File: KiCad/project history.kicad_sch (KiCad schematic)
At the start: 0 parts

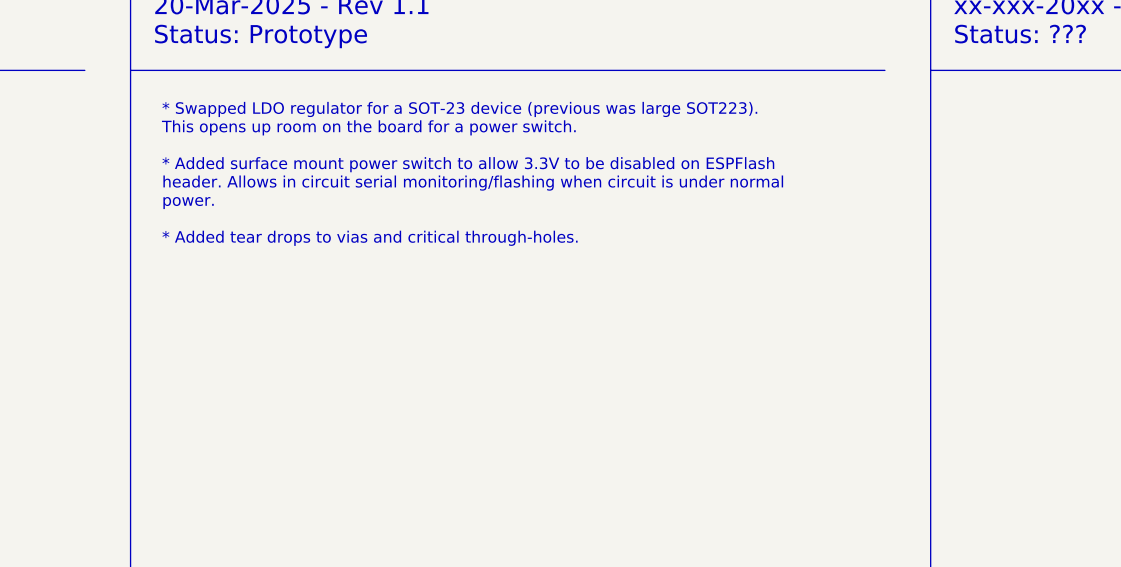
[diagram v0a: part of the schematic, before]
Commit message: Update BOM and general tidy-up
Include DigiKey cut-tape components and add flag to indicate own stocked items. Remove files that aren't part of the sharable project (KiCad 9 embeds), Remove empty/irrelevant folders.
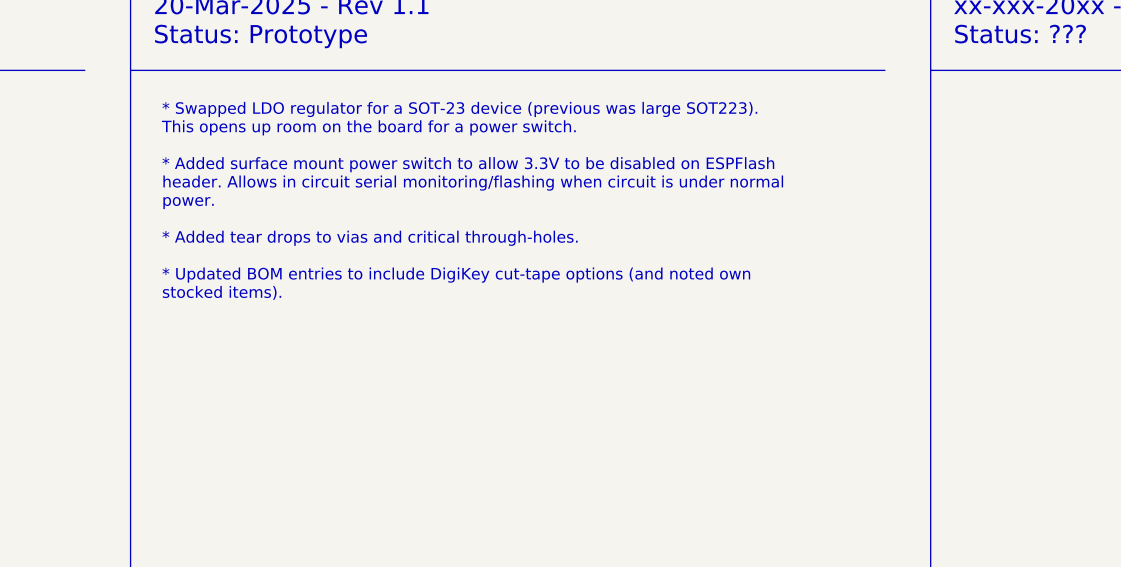
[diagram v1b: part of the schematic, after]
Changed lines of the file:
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@@
 		)
 	)
-	(text_box "* Swapped LDO regulator for a SOT-23 device (previous was large SOT223). This opens up room on the board for a power switch.\n\n* Added surface mount power switch to allow 3.3V to be disabled on ESPFlash header. Allows in circuit serial monitoring/flashing when circuit is under normal power.\n\n* Added tear drops to vias and critical through-holes."
+	(text_box "* Swapped LDO regulator for a SOT-23 device (previous was large SOT223). This opens up room on the board for a power switch.\n\n* Added surface mount power switch to allow 3.3V to be disabled on ESPFlash header. Allows in circuit serial monitoring/flashing when circuit is under normal power.\n\n* Added tear drops to vias and critical through-holes.\n\n* Updated BOM entries to include DigiKey cut-tape options (and noted own stocked items)."
 		(exclude_from_sim no)
 		(at 109.22 38.1 0)
